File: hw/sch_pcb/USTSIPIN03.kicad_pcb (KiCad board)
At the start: 2 copper layers, 70.6 x 50.3 mm, 107 parts, among them J1 HEADER_2x15, M1 HOLE, M2 HOLE, M3 HOLE, M4 HOLE, M5 RFShield_TwoPieces, Q1 2SK2394-6, U1 ISL21080CIH341Z-TK, U10 ISL21080DIH309, U11 AT24CS64-SSHM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

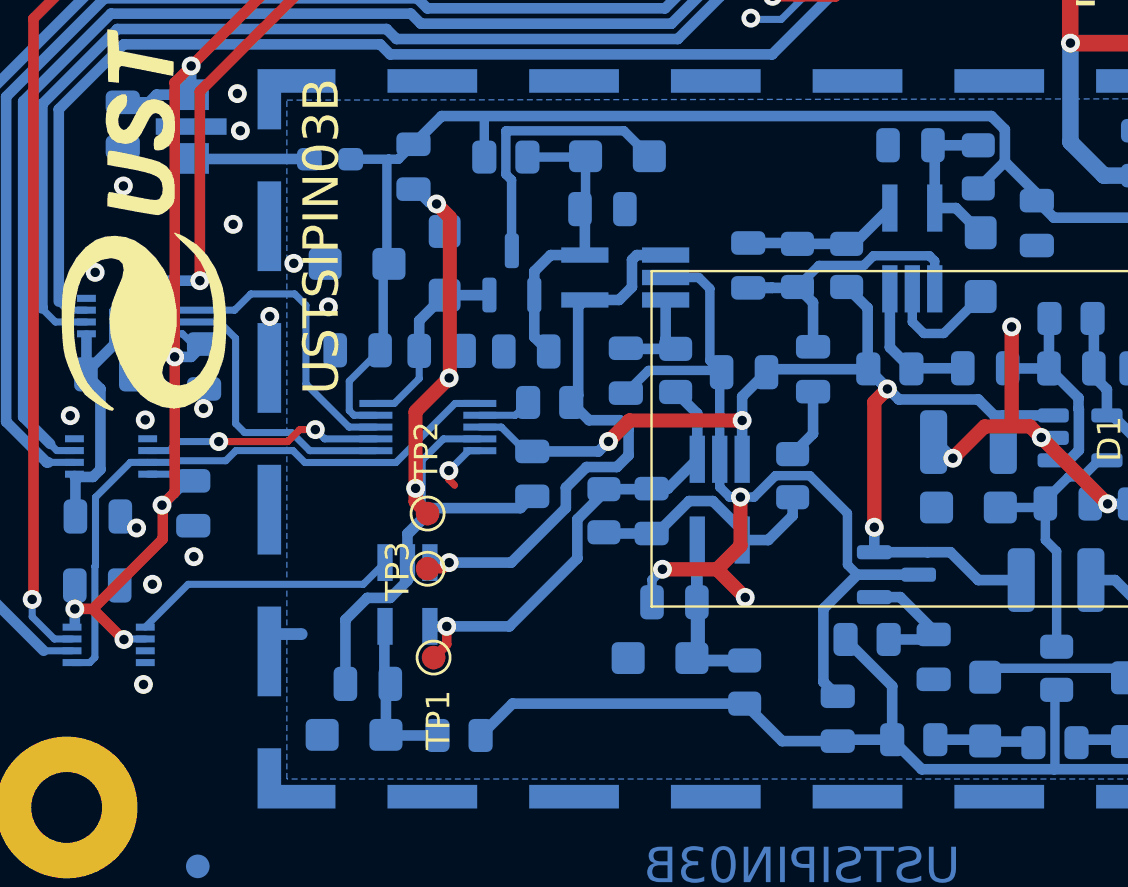
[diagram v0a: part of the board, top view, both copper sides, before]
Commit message: Removed hand-soldering footprints for OpAmps. Rosolve #1
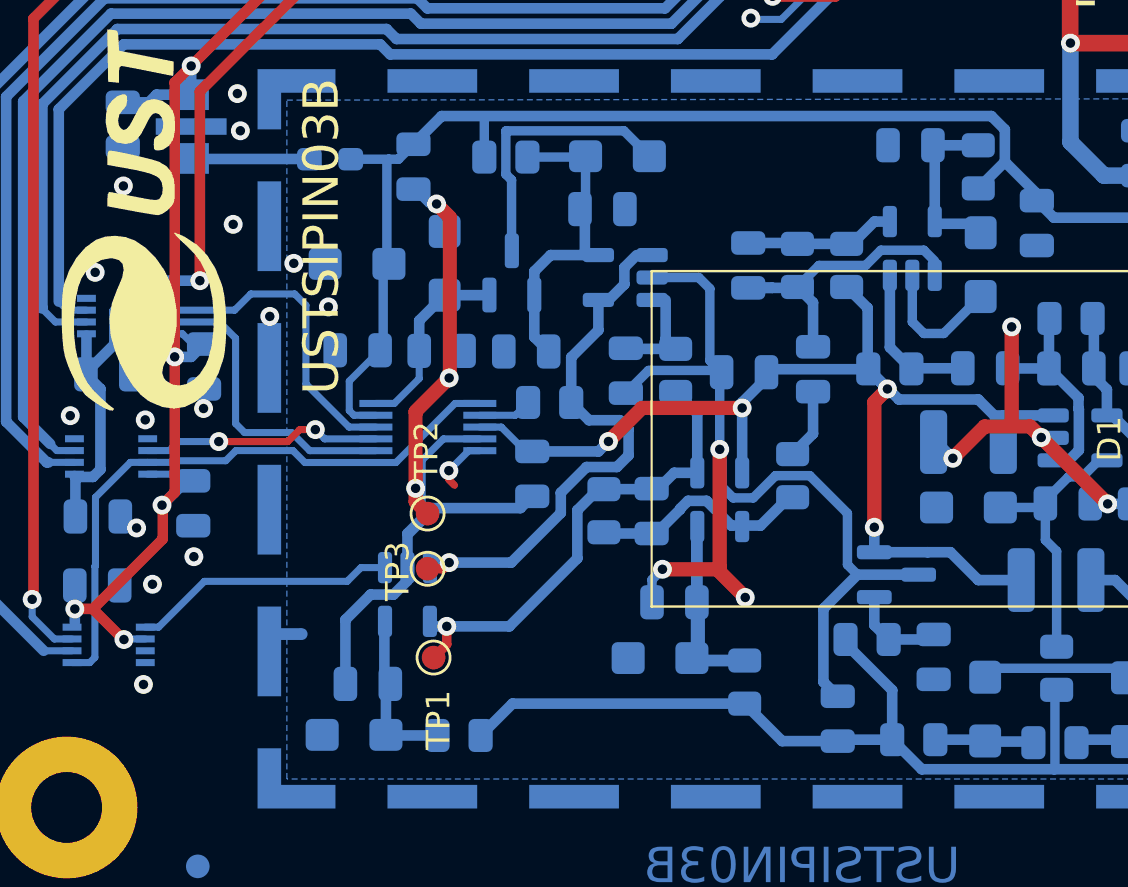
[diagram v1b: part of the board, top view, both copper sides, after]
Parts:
- U2, U4, U9: footprint Package_TO_SOT_SMD:TSOT-23-5_HandSoldering -> Package_TO_SOT_SMD:TSOT-23-5
- U6: footprint Package_TO_SOT_SMD:SOT-23-5_HandSoldering -> Package_TO_SOT_SMD:SOT-23-5
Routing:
- net Net-(U2--): track 25.6 -> 23.8 mm
- net Net-(U10-Vin): track 6.39 -> 4.80 mm
- net Net-(U4--): track 10.7 -> 9.53 mm
- net GNDA: track 127.4 -> 128.5 mm
- net Net-(C31-Pad2): track 13.7 -> 12.8 mm
